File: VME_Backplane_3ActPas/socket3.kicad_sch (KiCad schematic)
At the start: 7 parts, among them X101 DIN41612_03x32_ABC_VMEbus, X401A1 Jumper_2_Open, X401B1 Jumper_2_Open, X401C1 Jumper_2_Open, X401D1 Jumper_2_Open, X501 Jumper_2_Open

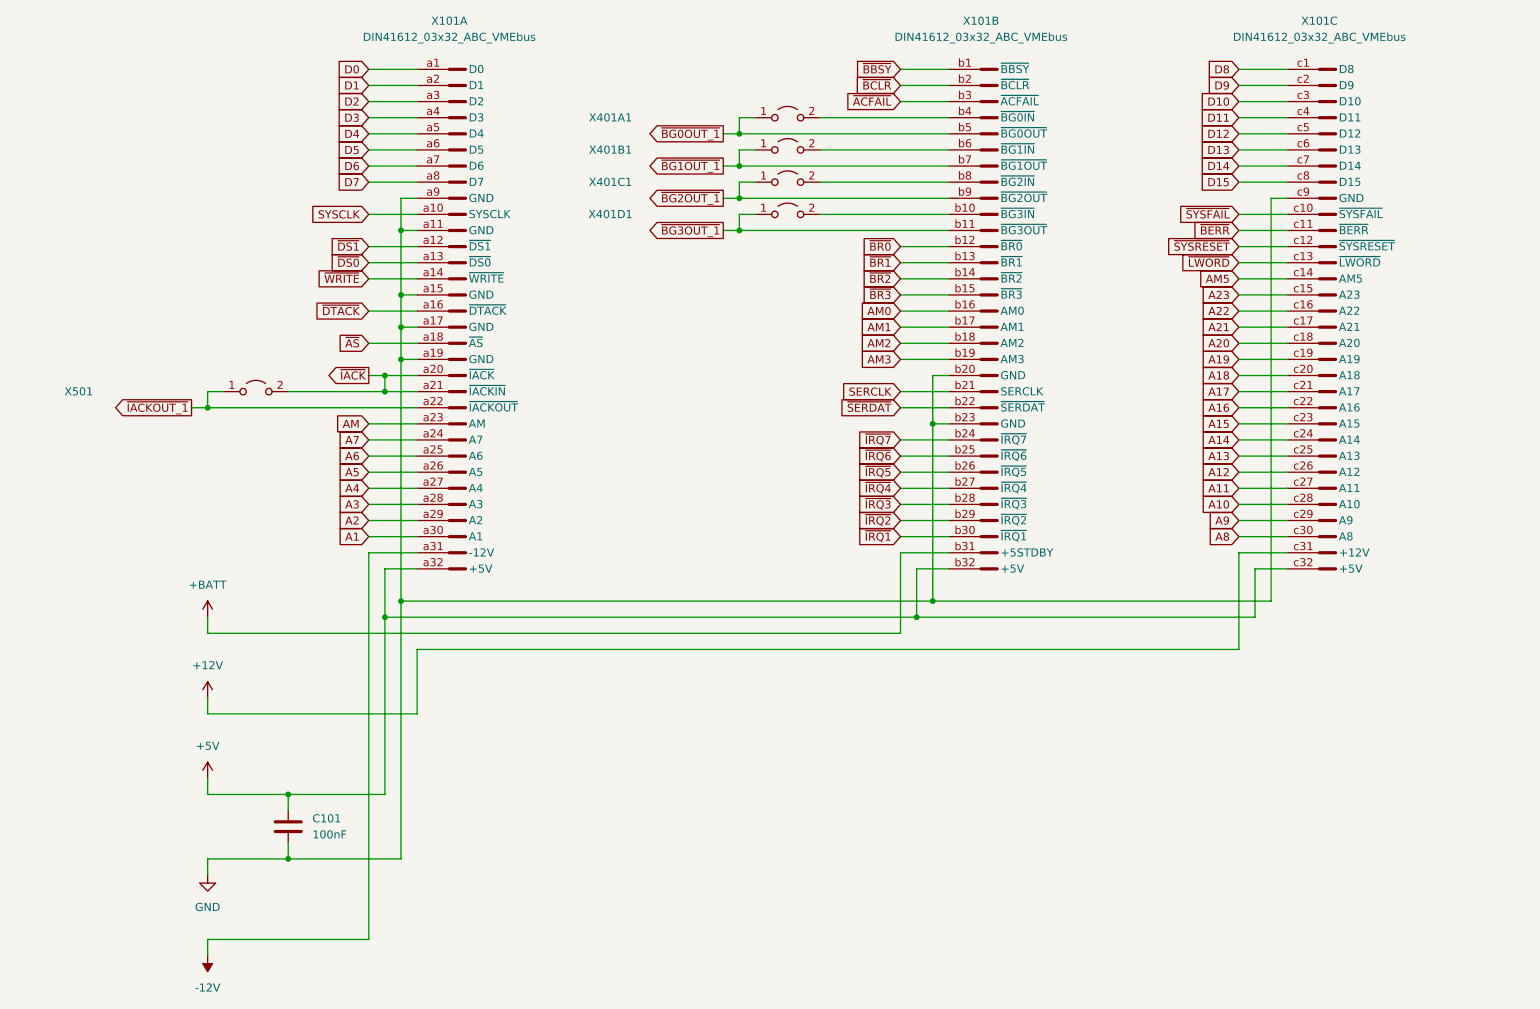
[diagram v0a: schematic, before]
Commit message: Expand schematics to 3 slots
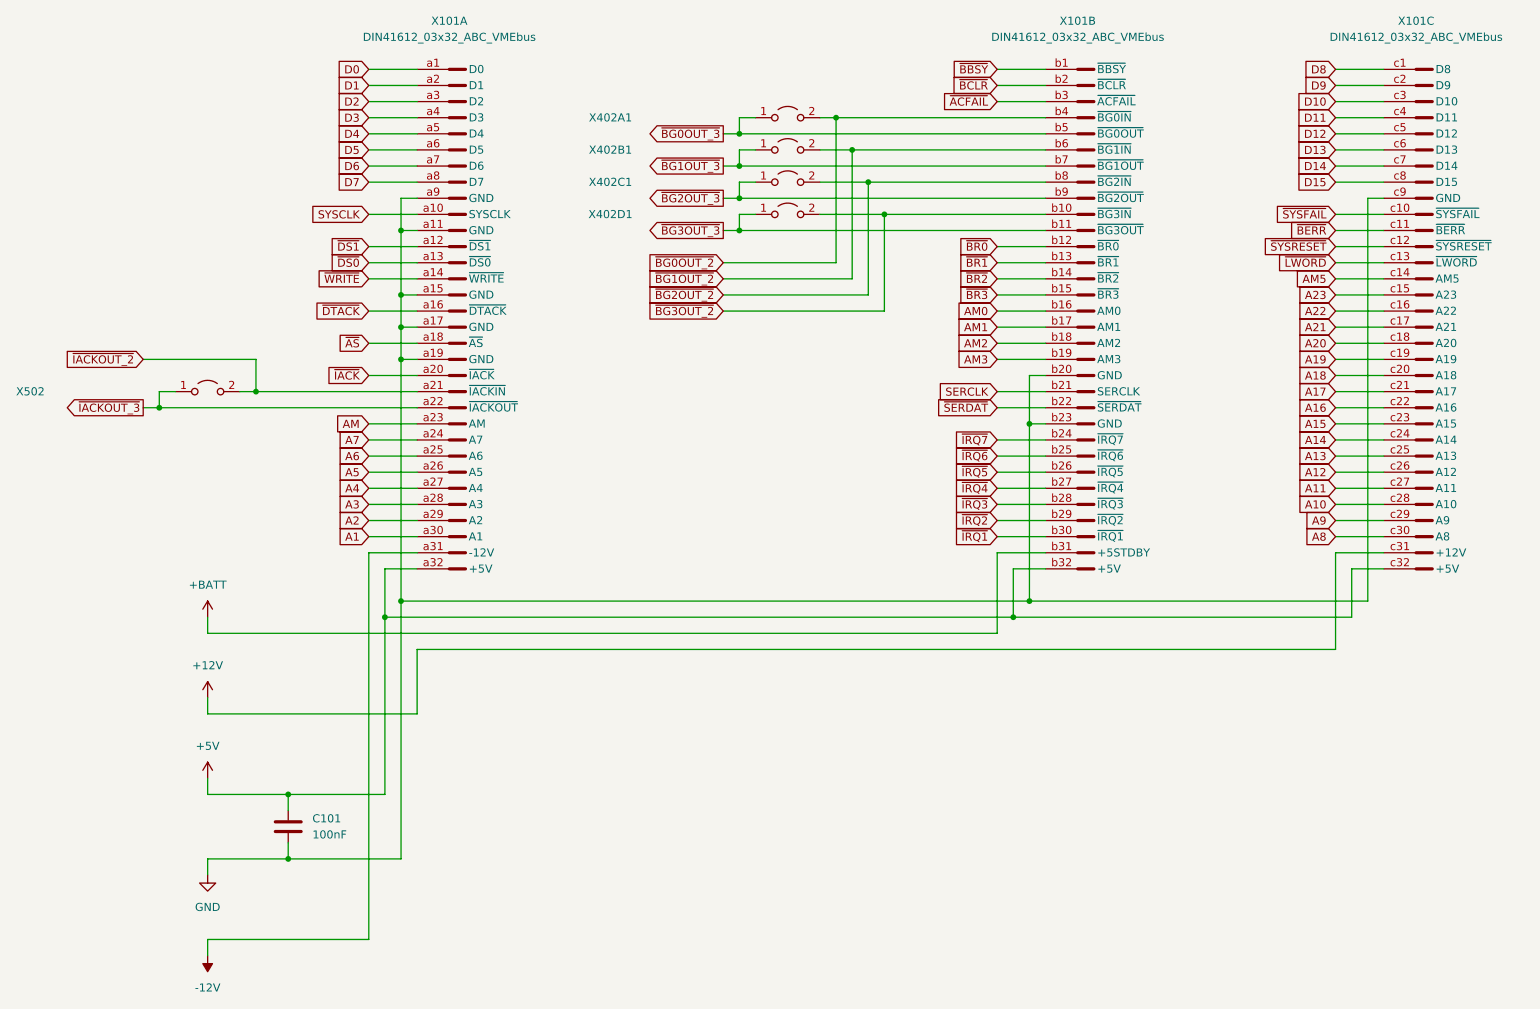
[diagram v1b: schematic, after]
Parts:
- renumbered X401A1 to X402A1, X401B1 to X402B1, X401C1 to X402C1, X401D1 to X402D1, X501 to X502
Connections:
- net ~{IACK}: no longer X101.a21 (~{IACKIN}), X502.2 (B)
- net ~{BG1OUT_2}: now reaches X101.b6 (~{BG1IN}), X402B1.2 (B)
- net ~{BG2OUT_2}: now reaches X101.b8 (~{BG2IN}), X402C1.2 (B)
- net ~{BG0OUT_2}: now reaches X101.b4 (~{BG0IN}), X402A1.2 (B)
- net ~{BG3OUT_2}: now reaches X101.b10 (~{BG3IN}), X402D1.2 (B)
- net ~{BG0OUT_1} renamed ~{BG0OUT_3}
- net ~{BG1OUT_1} renamed ~{BG1OUT_3}
- net ~{BG2OUT_1} renamed ~{BG2OUT_3}
- net ~{BG3OUT_1} renamed ~{BG3OUT_3}
- net ~{IACKOUT_1} renamed ~{IACKOUT_3}
- new net ~{IACKOUT_2}: X101.a21 (~{IACKIN}), X502.2 (B)
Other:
- moved on the sheet: X101B, X101C, X502
